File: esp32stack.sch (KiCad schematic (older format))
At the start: 26 parts, among them J1 CONN_01X17, J2 CONN_01X16, P1 USB_OTG, Q1 MMBT3904, Q2 MMBT3904, SW1 SWITCH_SPST, SW2 SWITCH_SPST, U1 ESP32-WROOM, U2 NCP1117ST33T3G, U3 CP2102

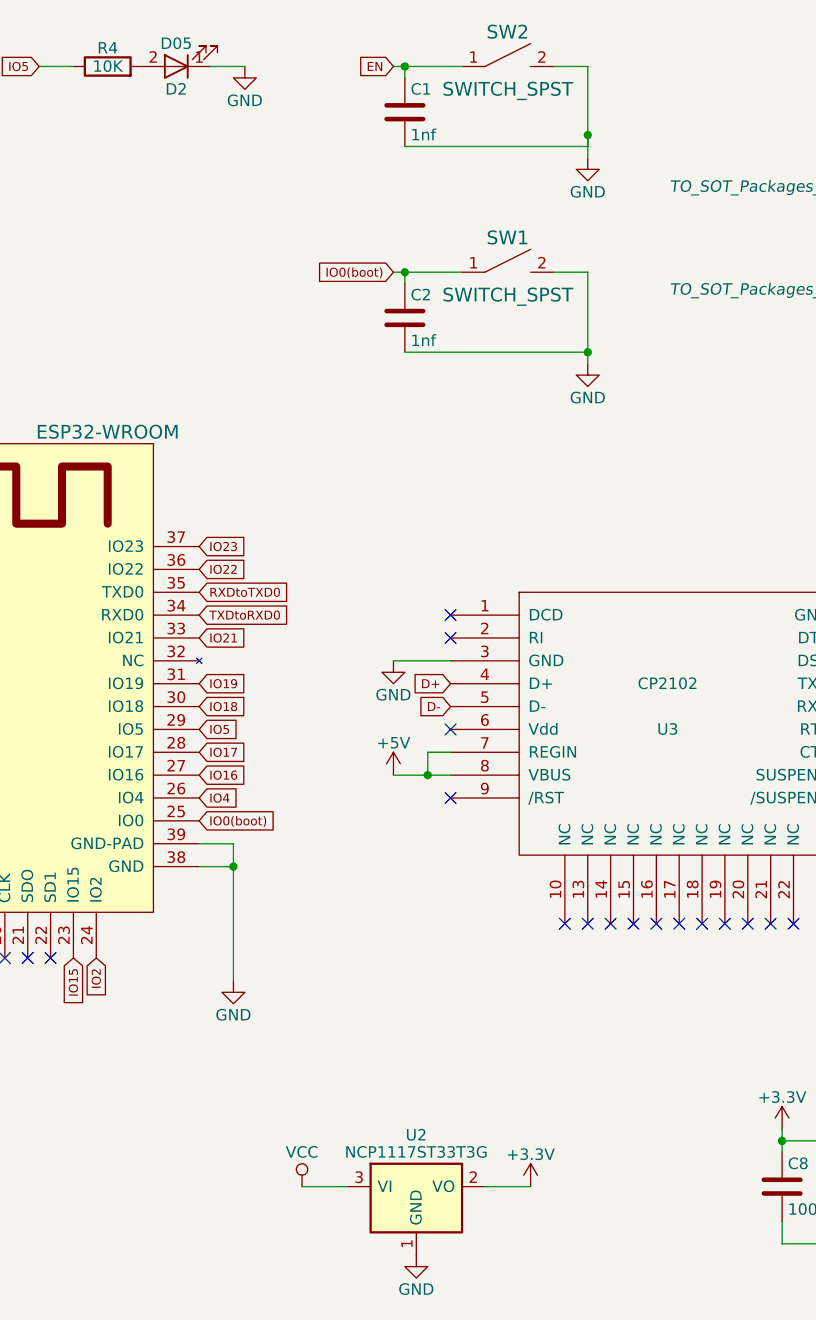
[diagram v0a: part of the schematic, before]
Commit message: Adjust hole position
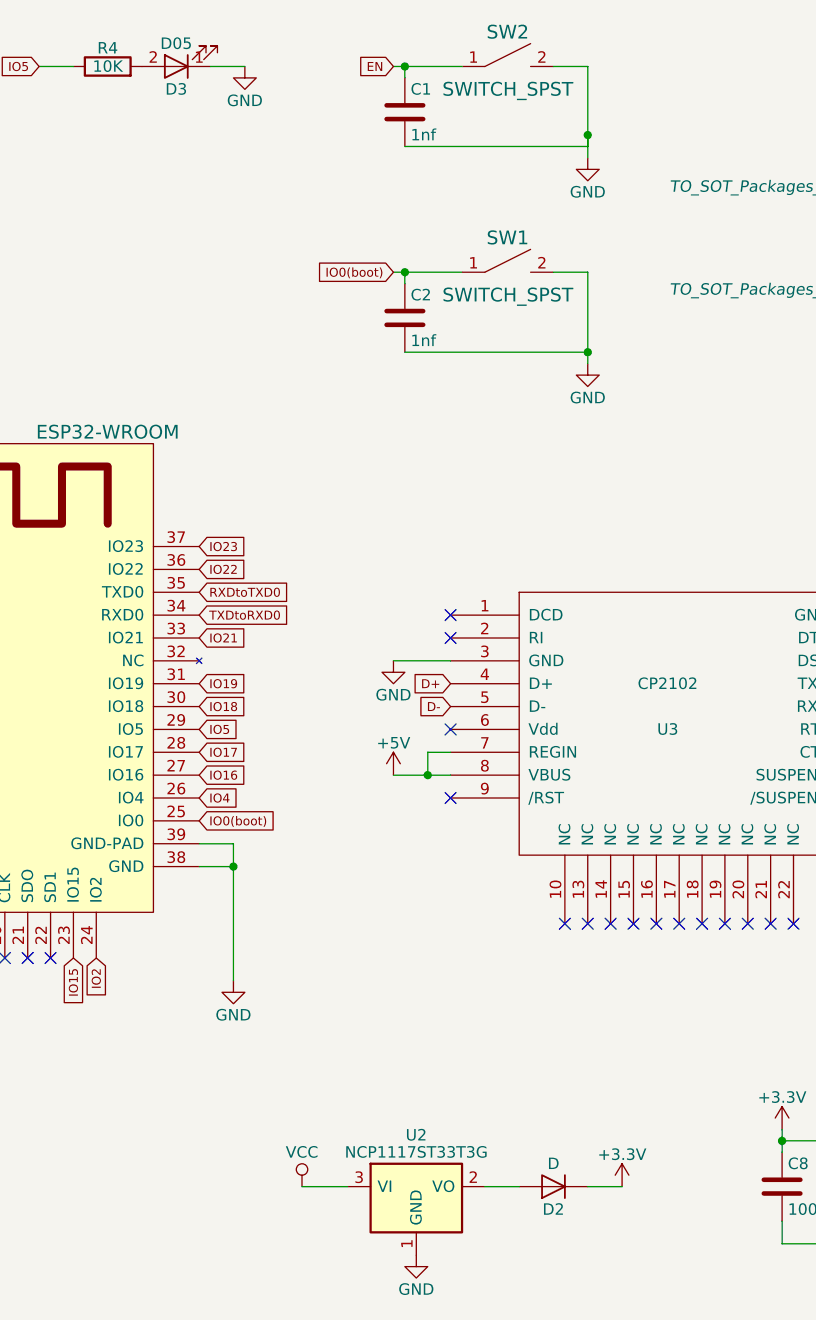
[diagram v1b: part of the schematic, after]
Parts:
- added D2: D, common:D_0805, symbol D
- D1: footprint Diodes_SMD:D_0805 -> common:D_0805
- renumbered D2 to D3
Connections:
- net +3V3: now also D2.1 (K); no longer U2.2 (VO)
- new net: D2.2 (A), U2.2 (VO)
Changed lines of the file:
@@
 L +3.3V #PWR06
 U 1 1 586B907B
-P 7850 5800
-F 0 "#PWR06" H 7850 5650 50  0001 C CNN
-F 1 "+3.3V" H 7850 5940 50  0000 C CNN
-F 2 "" H 7850 5800 50  0000 C CNN
-F 3 "" H 7850 5800 50  0000 C CNN
-	1    7850 5800
+P 8250 5800
+F 0 "#PWR06" H 8250 5650 50  0001 C CNN
+F 1 "+3.3V" H 8250 5940 50  0000 C CNN
+F 2 "" H 8250 5800 50  0000 C CNN
+F 3 "" H 8250 5800 50  0000 C CNN
+	1    8250 5800
 	1    0    0    -1
 $EndComp
@@
 F 0 "D1" H 10250 5700 50  0000 C CNN
 F 1 "D" H 10250 5500 50  0000 C CNN
-F 2 "Diodes_SMD:D_0805" H 10250 5600 50  0001 C CNN
+F 2 "common:D_0805" H 10250 5600 50  0001 C CNN
 F 3 "" H 10250 5600 50  0000 C CNN
 	1    10250 5600
@@
 $EndComp
 $Comp
-L LED D2
+L LED D3
 U 1 1 58AAE67A
 P 6300 900
-F 0 "D2" H 6300 1000 50  0000 C CNN
+F 0 "D3" H 6300 1000 50  0000 C CNN
 F 1 "D05" H 6300 800 50  0000 C CNN
 F 2 "LEDs:LED_0603" H 6300 900 50  0001 C CNN
@@
 	6850 5800 7050 5800
 Wire Wire Line
-	7650 5800 7850 5800
-Wire Wire Line
 	9500 3300 9900 3300
 Wire Wire Line
@@
 Wire Wire Line
 	3200 4350 3300 4350
+$Comp
+L D D2
+U 1 1 58F9822E
+P 7950 5800
+F 0 "D2" H 7950 5900 50  0000 C CNN
+F 1 "D" H 7950 5700 50  0000 C CNN
+F 2 "common:D_0805" H 7950 5800 50  0001 C CNN
+F 3 "" H 7950 5800 50  0000 C CNN
+	1    7950 5800
+	-1   0    0    1
+$EndComp
+Wire Wire Line
+	7650 5800 7800 5800
+Wire Wire Line
+	8100 5800 8250 5800
 $EndSCHEMATC
